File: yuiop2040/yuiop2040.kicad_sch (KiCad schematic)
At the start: 32 parts, among them J1 USB_B_Micro, SW1 BOOTSEL, SW2 RESET, U1 MIC5219-3.3YM5, U2 RP2040, U3 W25Q16JVSS, Y1 FA238V 12.000000MHz 10.0 +50.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

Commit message: YUIOP2040: RP2040 base controller board
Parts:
- removed SW1: BOOTSEL, symbol Switch:SW_Push
- removed SW2: RESET, symbol Switch:SW_Push
- added J2: USB_C_Receptacle_USB2.0, Connector_USB:USB_C_Receptacle_XKB_U262-16XN-4BVC11, symbol Connector:USB_C_Receptacle_USB2.0
- added J3, J4: Conn_01x20, Connector_PinHeader_2.54mm:PinHeader_1x20_P2.54mm_Vertical, symbol Connector_Generic:Conn_01x20
- added J5: Conn_01x03, Connector_PinHeader_2.54mm:PinHeader_1x03_P2.54mm_Vertical, symbol Connector_Generic:Conn_01x03
- added R31, R32: 5.1k, Resistor_SMD:R_0603_1608Metric, symbol Device:R_Small
- C1, C10, C11, C12, C13, C14, C15, C16, C17, C2, C3, C4, C5, C6, C7, C8, C9: footprint (none) -> Capacitor_SMD:C_0603_1608Metric
- DS1: footprint (none) -> Diode_SMD:D_SOD-123
- F1: footprint (none) -> Fuse:Fuse_1206_3216Metric
- J1: footprint (none) -> Connector_USB:USB_Micro-B_Amphenol_10103594-0001LF_Horizontal
- R1, R2, R3, R4, R5, R6: footprint (none) -> Resistor_SMD:R_0603_1608Metric
- Y1: footprint (none) -> Crystal:Crystal_SMD_SeikoEpson_FA238V-4Pin_3.2x2.5mm
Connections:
- net +3V3: now also J3.4 (Pin_4)
- net GND: now also J2.A1 (GND), J2.A12 (GND), J2.B1 (GND), J2.B12 (GND), J2.S1 (SHIELD), J3.2 (Pin_2), J4.2 (Pin_2), J4.20 (Pin_20), J5.2 (Pin_2), R31.2, R32.2
- net GPIO0: now also J3.5 (Pin_5)
- net GPIO1: now also J3.6 (Pin_6)
- net GPIO10: now also J3.15 (Pin_15)
- net GPIO11: now also J3.16 (Pin_16)
- net GPIO12: now also J3.17 (Pin_17)
- net GPIO13: now also J3.18 (Pin_18)
- net GPIO14: now also J3.19 (Pin_19)
- net GPIO15: now also J3.20 (Pin_20)
- net GPIO16: now also J4.3 (Pin_3)
- net GPIO17: now also J4.4 (Pin_4)
- net GPIO18: now also J4.5 (Pin_5)
- net GPIO19: now also J4.6 (Pin_6)
- net GPIO2: now also J3.7 (Pin_7)
- net GPIO20: now also J4.7 (Pin_7)
- net GPIO21: now also J4.8 (Pin_8)
- net GPIO22: now also J4.9 (Pin_9)
- net GPIO23: now also J4.10 (Pin_10)
- net GPIO24: now also J4.11 (Pin_11)
- net GPIO25: now also J4.12 (Pin_12)
- net GPIO26_ADC0: now also J4.13 (Pin_13)
- net GPIO27_ADC1: now also J4.14 (Pin_14)
- net GPIO28_ADC2: now also J4.15 (Pin_15)
- net GPIO29_ADC3: now also J4.16 (Pin_16)
- net GPIO3: now also J3.8 (Pin_8)
- net GPIO4: now also J3.9 (Pin_9)
- net GPIO5: now also J3.10 (Pin_10)
- net GPIO6: now also J3.11 (Pin_11)
- net GPIO7: now also J3.12 (Pin_12)
- net GPIO8: now also J3.13 (Pin_13)
- net GPIO9: now also J3.14 (Pin_14)
- net SWCLK: now also J5.1 (Pin_1)
- net SWD: now also J5.3 (Pin_3)
- net USB_D+: now also J2.A6 (D+), J2.B6 (D+), J4.19 (Pin_19)
- net USB_D-: now also J2.A7 (D-), J2.B7 (D-), J4.18 (Pin_18)
- net USB_VBUS: now also J2.A4 (VBUS), J2.A9 (VBUS), J2.B4 (VBUS), J2.B9 (VBUS), J4.17 (Pin_17)
- net VSYS: now also J3.3 (Pin_3)
- net RESET: now reaches R6.1
- net RESET: now also J4.1 (Pin_1)
- net BOOTSEL: now reaches R5.1
- net BOOTSEL: now also J3.1 (Pin_1)
- new net: J2.B5 (CC2), R32.1
- new net: J2.A5 (CC1), R31.1
- no-connect marks 2 -> 4
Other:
- title: RP2040 Controller -> YUIOP2040
- moved on the sheet: C1, C17, C2, C3, C4, C5, DS1, F1, J1, R3, R4, R5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

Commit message: yuiop2040: rev.2
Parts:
- U2: footprint RP2040_minimal:RP2040-QFN-56 -> RP2040_minimal:RP2040-QFN-56-r2
- U3: footprint Package_SO:SOIC-8_5.23x5.23mm_P1.27mm -> Package_SO:SOIC-8_3.9x4.9mm_P1.27mm
- renumbered R31 to R7, R32 to R8
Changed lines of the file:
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@@
   (title_block
     (title "YUIOP2040")
-    (date "2022-02-11")
-    (rev "1")
+    (date "2022-03-04")
+    (rev "2")
     (company "KaoriYa")
   )
@@
   (symbol (lib_id "Device:R_Small") (at 49.53 157.48 90) (unit 1)
     (in_bom yes) (on_board yes)
-    (property "Reference" "R32" (id 0) (at 46.99 160.02 90))
+    (property "Reference" "R8" (id 0) (at 46.99 160.02 90))
     (property "Value" "5.1k" (id 1) (at 53.34 160.02 90))
     (property "Footprint" "Resistor_SMD:R_0603_1608Metric" (id 2) (at 49.53 157.48 0)
@@
   (symbol (lib_id "Device:R_Small") (at 49.53 154.94 90) (unit 1)
     (in_bom yes) (on_board yes)
-    (property "Reference" "R31" (id 0) (at 46.99 152.4 90))
+    (property "Reference" "R7" (id 0) (at 46.99 152.4 90))
     (property "Value" "5.1k" (id 1) (at 53.34 152.4 90))
     (property "Footprint" "Resistor_SMD:R_0603_1608Metric" (id 2) (at 49.53 154.94 0)
@@
       (effects (font (size 1.27 1.27)) (justify left))
     )
-    (property "Footprint" "RP2040_minimal:RP2040-QFN-56" (id 2) (at 140.97 111.76 0)
+    (property "Footprint" "RP2040_minimal:RP2040-QFN-56-r2" (id 2) (at 140.97 111.76 0)
       (effects (font (size 1.27 1.27)) hide)
     )
@@
       (effects (font (size 1.27 1.27)) (justify left))
     )
-    (property "Footprint" "Package_SO:SOIC-8_5.23x5.23mm_P1.27mm" (id 2) (at 82.55 80.01 0)
+    (property "Footprint" "Package_SO:SOIC-8_3.9x4.9mm_P1.27mm" (id 2) (at 82.55 80.01 0)
       (effects (font (size 1.27 1.27)) hide)
     )
@@
     )
     (path "/17c04d46-5545-49e7-a7ea-176e2d24b709"
-      (reference "R31") (unit 1) (value "5.1k") (footprint "Resistor_SMD:R_0603_1608Metric")
+      (reference "R7") (unit 1) (value "5.1k") (footprint "Resistor_SMD:R_0603_1608Metric")
     )
     (path "/10cecd80-09b9-4583-b37c-5971b308307c"
-      (reference "R32") (unit 1) (value "5.1k") (footprint "Resistor_SMD:R_0603_1608Metric")
+      (reference "R8") (unit 1) (value "5.1k") (footprint "Resistor_SMD:R_0603_1608Metric")
     )
     (path "/2e584fe4-1621-4a64-ac2a-2ed01a0e9342"
@@
     )
     (path "/675274af-e6f4-43be-85d7-d6b1c6e80024"
-      (reference "U2") (unit 1) (value "RP2040") (footprint "RP2040_minimal:RP2040-QFN-56")
+      (reference "U2") (unit 1) (value "RP2040") (footprint "RP2040_minimal:RP2040-QFN-56-r2")
     )
     (path "/eb1c0ad7-0554-478d-b564-32d916be20bf"
-      (reference "U3") (unit 1) (value "W25Q16JVSS") (footprint "Package_SO:SOIC-8_5.23x5.23mm_P1.27mm")
+      (reference "U3") (unit 1) (value "W25Q16JVSS") (footprint "Package_SO:SOIC-8_3.9x4.9mm_P1.27mm")
     )
     (path "/d67216a7-4544-4493-ba76-2e90a2a63f74"

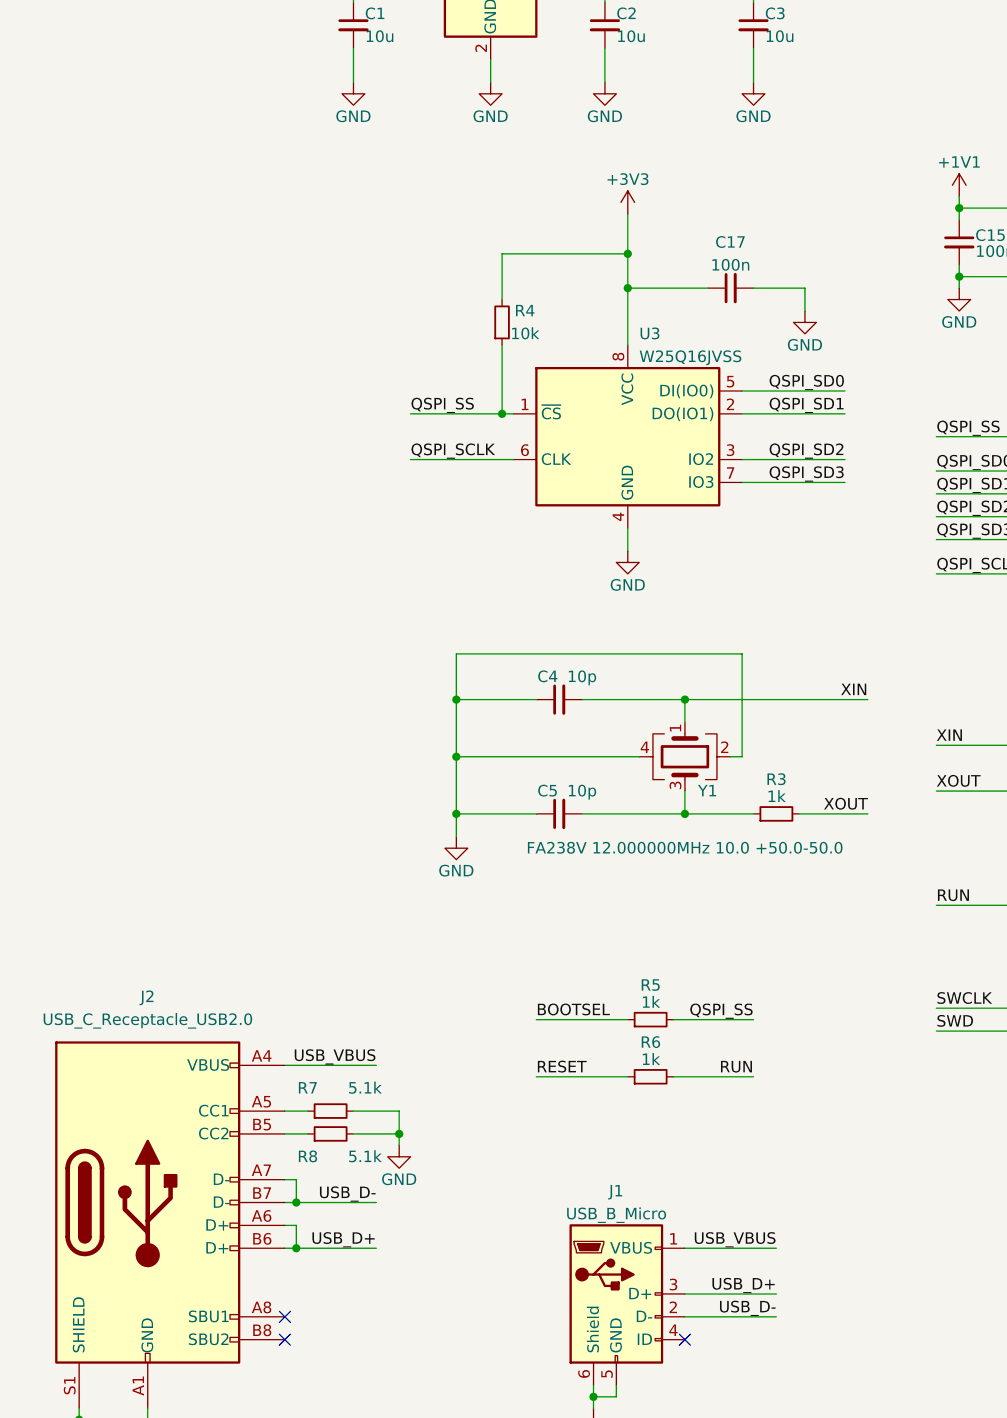
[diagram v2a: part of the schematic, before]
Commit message: convert yuiop2040 for KiCad 8
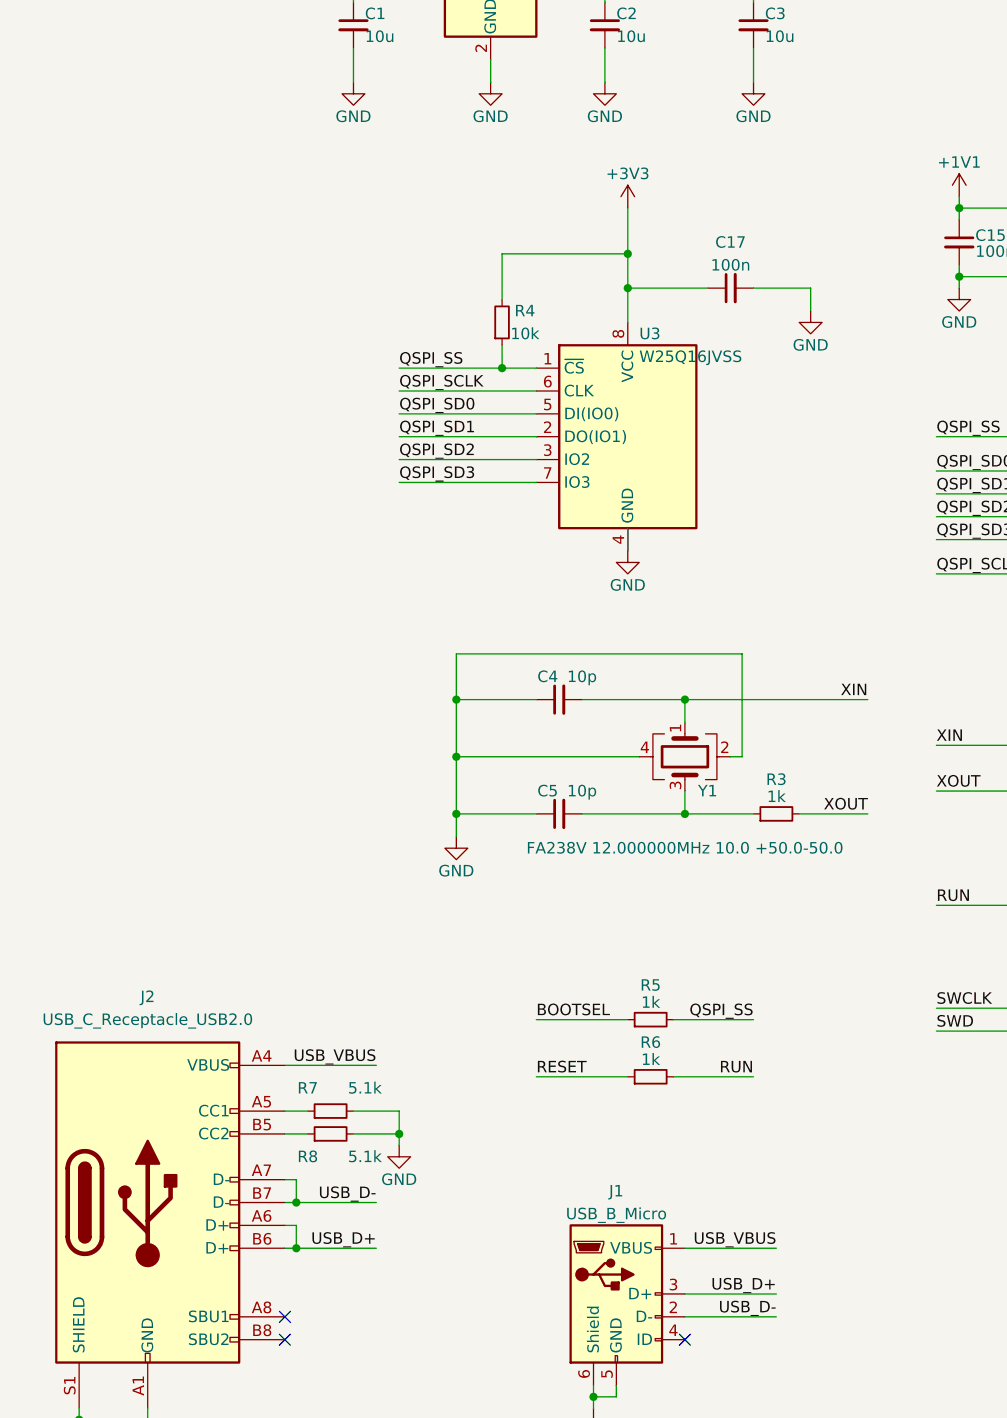
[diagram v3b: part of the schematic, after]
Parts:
- J2: symbol Connector:USB_C_Receptacle_USB2.0 -> Connector:USB_C_Receptacle_USB2.0_16P
- U2: footprint RP2040_minimal:RP2040-QFN-56-r2 -> RP2040_minimal:RP2040-QFN-56
- U3: footprint Package_SO:SOIC-8_3.9x4.9mm_P1.27mm -> Package_SO:SOIC-8_5.23x5.23mm_P1.27mm
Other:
- moved on the sheet: U3
